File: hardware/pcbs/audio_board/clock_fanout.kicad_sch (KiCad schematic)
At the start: 10 parts, among them U6 TAA3040

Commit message: prepare for clock fanout
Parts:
- removed C30, C33, C36: 1μF, Capacitor_SMD:C_0805_2012Metric, symbol Device:C_Small
- removed C31, C38: 10μF, Capacitor_SMD:C_0805_2012Metric, symbol Device:C_Small
- removed C32, C34, C35, C37: 100nF, Capacitor_SMD:C_0805_2012Metric, symbol Device:C_Small
- removed U6: TAA3040, ics:WQFN-24-1EP_4x4mm_P0.5mm_EP2.6x2.6mm, symbol audio_ics:TAA3040
- added C57, C58, C59: 1μF, Capacitor_SMD:C_0805_2012Metric, symbol Device:C_Small
- added FB1: FerriteBead_Small, Inductor_SMD:L_0805_2012Metric, symbol Device:FerriteBead_Small
- added R63, R64: 10kΩ, Resistor_SMD:R_0805_2012Metric, symbol Device:R
- added R65, R66, R67, R68, R69, R70: 0Ω, Resistor_SMD:R_0805_2012Metric, symbol Device:R
- added R71, R72, R73, R74, R75, R76: 47Ω, Resistor_SMD:R_0805_2012Metric, symbol Device:R
- added U7, U8: LMK1C1103A, Package_SO:TSSOP-8_4.4x3mm_P0.65mm, symbol ics:LMK1C1104A
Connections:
- net +3.3V: now also C57.1, FB1.1
- net BCLK: now also R65.2, R66.2, R67.2, U7.1 (CLKIN)
- net GND: now also C57.2, C58.2, C59.2, U7.4 (GND), U8.4 (GND)
- new net: C58.1, C59.1, FB1.2, R63.1, R64.1, U7.6 (VDD), U8.6 (VDD)
- new net: R63.2, U7.2 (1G)
- new net: R64.2, U8.2 (1G)
- new net: R70.1, R74.2, U8.3 (Y0)
- new net: R68.1, R76.2, U8.5 (Y2)
- new net: R69.1, R75.2, U8.8 (Y1)
- new net: R66.1, R72.2, U7.8 (Y1)
- new net: R65.1, R73.2, U7.5 (Y2)
- new net: R67.1, R71.2, U7.3 (Y0)
- new net BCLK1: R71.1
- new net BCLK2: R72.1
- new net BCLK3: R73.1
- new net LRCLK: R68.2, R69.2, R70.2, U8.1 (CLKIN)
- new net LRCLK1: R74.1
- new net LRCLK2: R75.1
- new net LRCLK3: R76.1

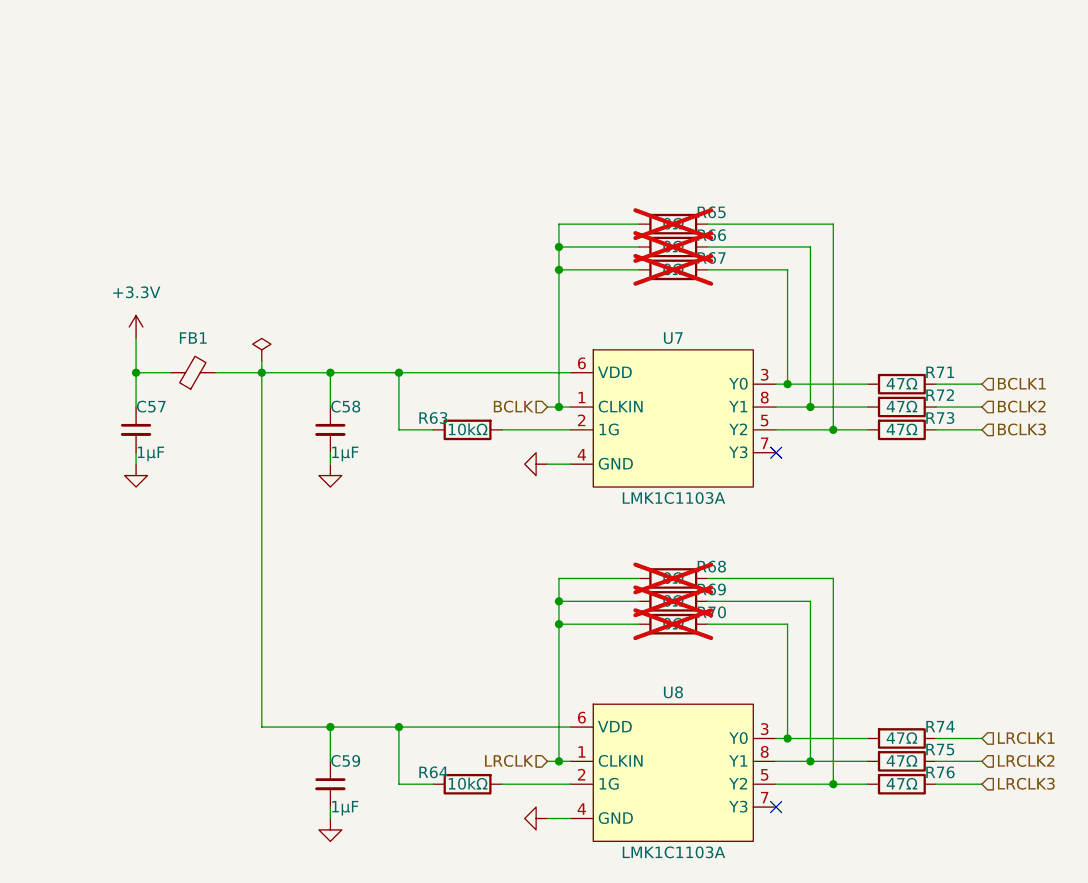
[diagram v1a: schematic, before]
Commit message: audioboard: route clock fanout
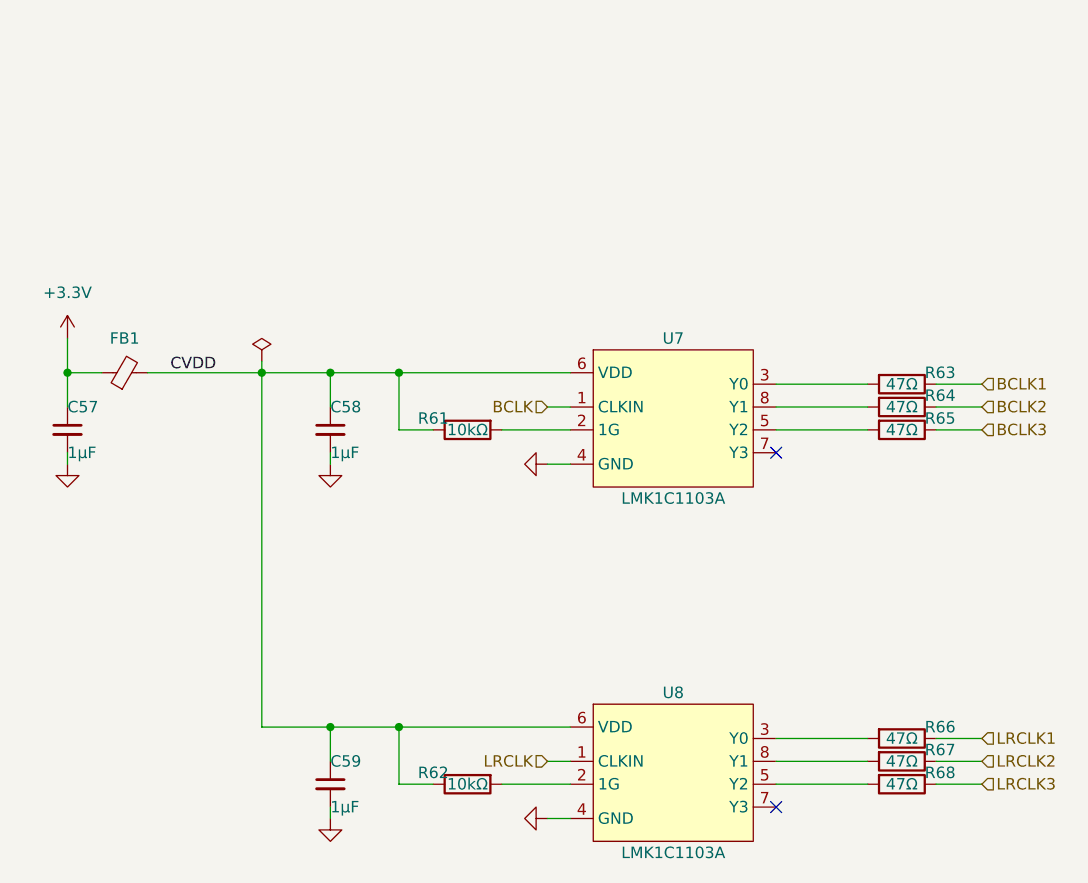
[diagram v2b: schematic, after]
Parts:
- removed R65, R66, R67, R68, R69, R70: 0Ω, Resistor_SMD:R_0805_2012Metric, symbol Device:R
- renumbered R63 to R61, R64 to R62, R71 to R63, R72 to R64, R73 to R65, R74 to R66, R75 to R67, R76 to R68
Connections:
- net CVDD: now reaches C58.1, C59.1, FB1.2, R61.1, R62.1, U7.6 (VDD), U8.6 (VDD)
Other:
- moved on the sheet: C57, FB1

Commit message: audioboard: finalise routing
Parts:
- renumbered R61 to R63, R62 to R64, R63 to R65, R64 to R66, R65 to R67, R66 to R68, R67 to R69, R68 to R70
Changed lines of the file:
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@@
 		(in_pos_files yes)
 		(dnp no)
-		(property "Reference" "R61"
+		(property "Reference" "R63"
 			(at 135.89 87.63 90)
 			(show_name no)
@@
 			(project "audio_board"
 				(path "/54443f96-c7c5-4432-b890-45b14a1547a1/ed335575-207f-4eab-bd63-8c911fac4ba1"
-					(reference "R61")
+					(reference "R63")
 					(unit 1)
 				)
@@
 		(in_pos_files yes)
 		(dnp no)
-		(property "Reference" "R66"
+		(property "Reference" "R68"
 			(at 190.5 121.92 90)
 			(show_name no)
@@
 			(project "audio_board"
 				(path "/54443f96-c7c5-4432-b890-45b14a1547a1/ed335575-207f-4eab-bd63-8c911fac4ba1"
-					(reference "R66")
+					(reference "R68")
 					(unit 1)
 				)
@@
 		(dnp no)
 		(fields_autoplaced yes)
-		(property "Reference" "#PWR0124"
+		(property "Reference" "#PWR0125"
 			(at 142.24 132.08 0)
 			(hide yes)
@@
 			(project "audio_board"
 				(path "/54443f96-c7c5-4432-b890-45b14a1547a1/ed335575-207f-4eab-bd63-8c911fac4ba1"
-					(reference "#PWR0124")
+					(reference "#PWR0125")
 					(unit 1)
 				)
@@
 		(dnp no)
 		(fields_autoplaced yes)
-		(property "Reference" "#PWR0121"
+		(property "Reference" "#PWR0122"
 			(at 124.46 99.06 0)
 			(hide yes)
@@
 			(project "audio_board"
 				(path "/54443f96-c7c5-4432-b890-45b14a1547a1/ed335575-207f-4eab-bd63-8c911fac4ba1"
-					(reference "#PWR0121")
+					(reference "#PWR0122")
 					(unit 1)
 				)
@@
 		(in_pos_files yes)
 		(dnp no)
-		(property "Reference" "R65"
+		(property "Reference" "R67"
 			(at 190.5 87.63 90)
 			(show_name no)
@@
 			(project "audio_board"
 				(path "/54443f96-c7c5-4432-b890-45b14a1547a1/ed335575-207f-4eab-bd63-8c911fac4ba1"
-					(reference "R65")
+					(reference "R67")
 					(unit 1)
 				)
@@
 		(in_pos_files yes)
 		(dnp no)
-		(property "Reference" "R62"
+		(property "Reference" "R64"
 			(at 135.89 127 90)
 			(show_name no)
@@
 			(project "audio_board"
 				(path "/54443f96-c7c5-4432-b890-45b14a1547a1/ed335575-207f-4eab-bd63-8c911fac4ba1"
-					(reference "R62")
+					(reference "R64")
 					(unit 1)
 				)
@@
 		(in_pos_files yes)
 		(dnp no)
-		(property "Reference" "R68"
+		(property "Reference" "R70"
 			(at 190.5 127 90)
 			(show_name no)
@@
 			(project "audio_board"
 				(path "/54443f96-c7c5-4432-b890-45b14a1547a1/ed335575-207f-4eab-bd63-8c911fac4ba1"
-					(reference "R68")
+					(reference "R70")
 					(unit 1)
 				)
@@
 		(dnp no)
 		(fields_autoplaced yes)
-		(property "Reference" "#PWR0122"
+		(property "Reference" "#PWR0123"
 			(at 124.46 138.43 0)
 			(hide yes)
@@
 			(project "audio_board"
 				(path "/54443f96-c7c5-4432-b890-45b14a1547a1/ed335575-207f-4eab-bd63-8c911fac4ba1"
-					(reference "#PWR0122")
+					(reference "#PWR0123")
 					(unit 1)
 				)
@@
 		(in_pos_files yes)
 		(dnp no)
-		(property "Reference" "R63"
+		(property "Reference" "R65"
 			(at 190.5 82.55 90)
 			(show_name no)
@@
 			(project "audio_board"
 				(path "/54443f96-c7c5-4432-b890-45b14a1547a1/ed335575-207f-4eab-bd63-8c911fac4ba1"
-					(reference "R63")
+					(reference "R65")
 					(unit 1)
 				)
@@
 		(dnp no)
 		(fields_autoplaced yes)
-		(property "Reference" "#PWR0123"
+		(property "Reference" "#PWR0124"
 			(at 142.24 92.71 0)
 			(hide yes)
@@
 			(project "audio_board"
 				(path "/54443f96-c7c5-4432-b890-45b14a1547a1/ed335575-207f-4eab-bd63-8c911fac4ba1"
-					(reference "#PWR0123")
+					(reference "#PWR0124")
 					(unit 1)
 				)
@@
 		(dnp no)
 		(fields_autoplaced yes)
-		(property "Reference" "#PWR0120"
+		(property "Reference" "#PWR0121"
 			(at 95.25 99.06 0)
 			(hide yes)
@@
 			(project "audio_board"
 				(path "/54443f96-c7c5-4432-b890-45b14a1547a1/ed335575-207f-4eab-bd63-8c911fac4ba1"
-					(reference "#PWR0120")
+					(reference "#PWR0121")
 					(unit 1)
 				)
@@
 		(in_pos_files yes)
 		(dnp no)
-		(property "Reference" "R67"
+		(property "Reference" "R69"
 			(at 190.5 124.46 90)
 			(show_name no)
@@
 			(project "audio_board"
 				(path "/54443f96-c7c5-4432-b890-45b14a1547a1/ed335575-207f-4eab-bd63-8c911fac4ba1"
-					(reference "R67")
+					(reference "R69")
 					(unit 1)
 				)
@@
 		(dnp no)
 		(fields_autoplaced yes)
-		(property "Reference" "#PWR0119"
+		(property "Reference" "#PWR0120"
 			(at 95.25 82.55 0)
 			(hide yes)
@@
 			(project "audio_board"
 				(path "/54443f96-c7c5-4432-b890-45b14a1547a1/ed335575-207f-4eab-bd63-8c911fac4ba1"
-					(reference "#PWR0119")
+					(reference "#PWR0120")
 					(unit 1)
 				)
@@
 		(in_pos_files yes)
 		(dnp no)
-		(property "Reference" "R64"
+		(property "Reference" "R66"
 			(at 190.5 85.09 90)
 			(show_name no)
@@
 			(project "audio_board"
 				(path "/54443f96-c7c5-4432-b890-45b14a1547a1/ed335575-207f-4eab-bd63-8c911fac4ba1"
-					(reference "R64")
-					(unit 1)
-				)
+					(reference "R66")
+					(unit 1)
+				)

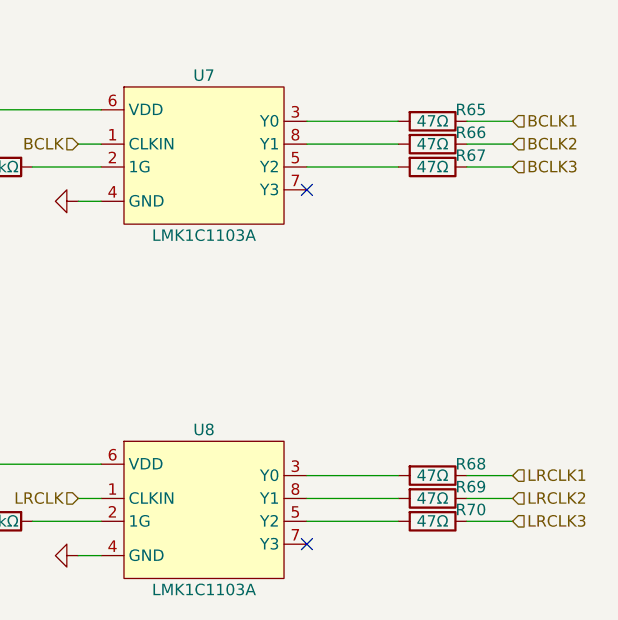
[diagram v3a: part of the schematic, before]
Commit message: audioboard: add bridges to clock fanout chips
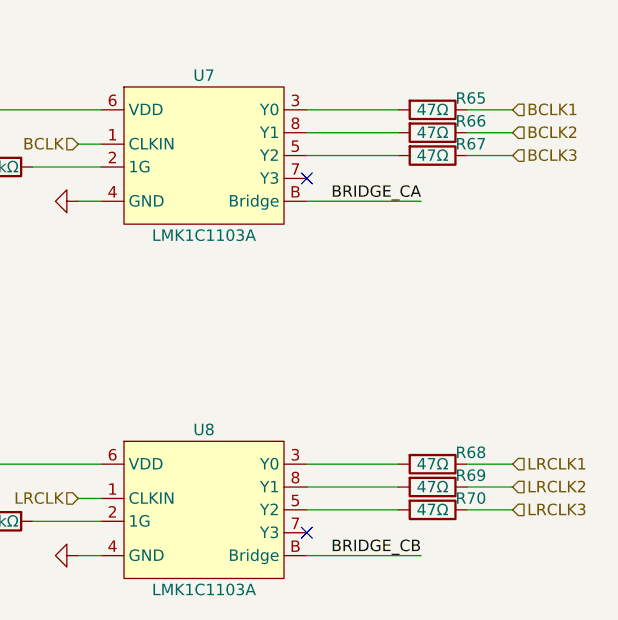
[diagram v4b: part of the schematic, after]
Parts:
- U7, U8: footprint Package_SO:TSSOP-8_4.4x3mm_P0.65mm -> ics:TSSOP-8_4.4x3mm_P0.65mm_bridges
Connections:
- new net BRIDGE_CA: U7.B (Bridge)
- new net BRIDGE_CB: U8.B (Bridge)
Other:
- moved on the sheet: R65, R66, R67, R68, R69, R70

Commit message: minor changes to audioboard
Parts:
- renumbered R63 to R61, R64 to R62, R65 to R63, R66 to R64, R67 to R65, R68 to R66, R69 to R67, R70 to R68
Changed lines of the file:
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@@
 		(in_pos_files yes)
 		(dnp no)
-		(property "Reference" "R63"
+		(property "Reference" "R61"
 			(at 135.89 87.63 90)
 			(show_name no)
@@
 			(project "audio_board"
 				(path "/54443f96-c7c5-4432-b890-45b14a1547a1/ed335575-207f-4eab-bd63-8c911fac4ba1"
-					(reference "R63")
+					(reference "R61")
 					(unit 1)
 				)
@@
 		(in_pos_files yes)
 		(dnp no)
-		(property "Reference" "R68"
+		(property "Reference" "R66"
 			(at 190.5 120.65 90)
 			(show_name no)
@@
 			(project "audio_board"
 				(path "/54443f96-c7c5-4432-b890-45b14a1547a1/ed335575-207f-4eab-bd63-8c911fac4ba1"
-					(reference "R68")
+					(reference "R66")
 					(unit 1)
 				)
@@
 		(dnp no)
 		(fields_autoplaced yes)
-		(property "Reference" "#PWR0125"
+		(property "Reference" "#PWR0121"
 			(at 142.24 132.08 0)
 			(hide yes)
@@
 			(project "audio_board"
 				(path "/54443f96-c7c5-4432-b890-45b14a1547a1/ed335575-207f-4eab-bd63-8c911fac4ba1"
-					(reference "#PWR0125")
+					(reference "#PWR0121")
 					(unit 1)
 				)
@@
 		(dnp no)
 		(fields_autoplaced yes)
-		(property "Reference" "#PWR0122"
+		(property "Reference" "#PWR0118"
 			(at 124.46 99.06 0)
 			(hide yes)
@@
 			(project "audio_board"
 				(path "/54443f96-c7c5-4432-b890-45b14a1547a1/ed335575-207f-4eab-bd63-8c911fac4ba1"
-					(reference "#PWR0122")
+					(reference "#PWR0118")
 					(unit 1)
 				)
@@
 		(in_pos_files yes)
 		(dnp no)
-		(property "Reference" "R67"
+		(property "Reference" "R65"
 			(at 190.5 86.36 90)
 			(show_name no)
@@
 			(project "audio_board"
 				(path "/54443f96-c7c5-4432-b890-45b14a1547a1/ed335575-207f-4eab-bd63-8c911fac4ba1"
-					(reference "R67")
+					(reference "R65")
 					(unit 1)
 				)
@@
 		(in_pos_files yes)
 		(dnp no)
-		(property "Reference" "R64"
+		(property "Reference" "R62"
 			(at 135.89 127 90)
 			(show_name no)
@@
 			(project "audio_board"
 				(path "/54443f96-c7c5-4432-b890-45b14a1547a1/ed335575-207f-4eab-bd63-8c911fac4ba1"
-					(reference "R64")
+					(reference "R62")
 					(unit 1)
 				)
@@
 		(in_pos_files yes)
 		(dnp no)
-		(property "Reference" "R70"
+		(property "Reference" "R68"
 			(at 190.5 125.73 90)
 			(show_name no)
@@
 			(project "audio_board"
 				(path "/54443f96-c7c5-4432-b890-45b14a1547a1/ed335575-207f-4eab-bd63-8c911fac4ba1"
-					(reference "R70")
+					(reference "R68")
 					(unit 1)
 				)
@@
 		(dnp no)
 		(fields_autoplaced yes)
-		(property "Reference" "#PWR0123"
+		(property "Reference" "#PWR0119"
 			(at 124.46 138.43 0)
 			(hide yes)
@@
 			(project "audio_board"
 				(path "/54443f96-c7c5-4432-b890-45b14a1547a1/ed335575-207f-4eab-bd63-8c911fac4ba1"
-					(reference "#PWR0123")
+					(reference "#PWR0119")
 					(unit 1)
 				)
@@
 		(in_pos_files yes)
 		(dnp no)
-		(property "Reference" "R65"
+		(property "Reference" "R63"
 			(at 190.5 81.28 90)
 			(show_name no)
@@
 			(project "audio_board"
 				(path "/54443f96-c7c5-4432-b890-45b14a1547a1/ed335575-207f-4eab-bd63-8c911fac4ba1"
-					(reference "R65")
+					(reference "R63")
 					(unit 1)
 				)
@@
 		(dnp no)
 		(fields_autoplaced yes)
-		(property "Reference" "#PWR0124"
+		(property "Reference" "#PWR0120"
 			(at 142.24 92.71 0)
 			(hide yes)
@@
 			(project "audio_board"
 				(path "/54443f96-c7c5-4432-b890-45b14a1547a1/ed335575-207f-4eab-bd63-8c911fac4ba1"
-					(reference "#PWR0124")
+					(reference "#PWR0120")
 					(unit 1)
 				)
@@
 		(dnp no)
 		(fields_autoplaced yes)
-		(property "Reference" "#PWR0121"
+		(property "Reference" "#PWR0117"
 			(at 95.25 99.06 0)
 			(hide yes)
@@
 			(project "audio_board"
 				(path "/54443f96-c7c5-4432-b890-45b14a1547a1/ed335575-207f-4eab-bd63-8c911fac4ba1"
-					(reference "#PWR0121")
+					(reference "#PWR0117")
 					(unit 1)
 				)
@@
 		(in_pos_files yes)
 		(dnp no)
-		(property "Reference" "R69"
+		(property "Reference" "R67"
 			(at 190.5 123.19 90)
 			(show_name no)
@@
 			(project "audio_board"
 				(path "/54443f96-c7c5-4432-b890-45b14a1547a1/ed335575-207f-4eab-bd63-8c911fac4ba1"
-					(reference "R69")
+					(reference "R67")
 					(unit 1)
 				)
@@
 		(dnp no)
 		(fields_autoplaced yes)
-		(property "Reference" "#PWR0120"
+		(property "Reference" "#PWR0116"
 			(at 95.25 82.55 0)
 			(hide yes)
@@
 			(project "audio_board"
 				(path "/54443f96-c7c5-4432-b890-45b14a1547a1/ed335575-207f-4eab-bd63-8c911fac4ba1"
-					(reference "#PWR0120")
+					(reference "#PWR0116")
 					(unit 1)
 				)
@@
 		(in_pos_files yes)
 		(dnp no)
-		(property "Reference" "R66"
+		(property "Reference" "R64"
 			(at 190.5 83.82 90)
 			(show_name no)
@@
 			(project "audio_board"
 				(path "/54443f96-c7c5-4432-b890-45b14a1547a1/ed335575-207f-4eab-bd63-8c911fac4ba1"
-					(reference "R66")
-					(unit 1)
-				)
+					(reference "R64")
+					(unit 1)
+				)
